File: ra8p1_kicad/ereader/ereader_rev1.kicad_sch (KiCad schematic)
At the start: 0 parts

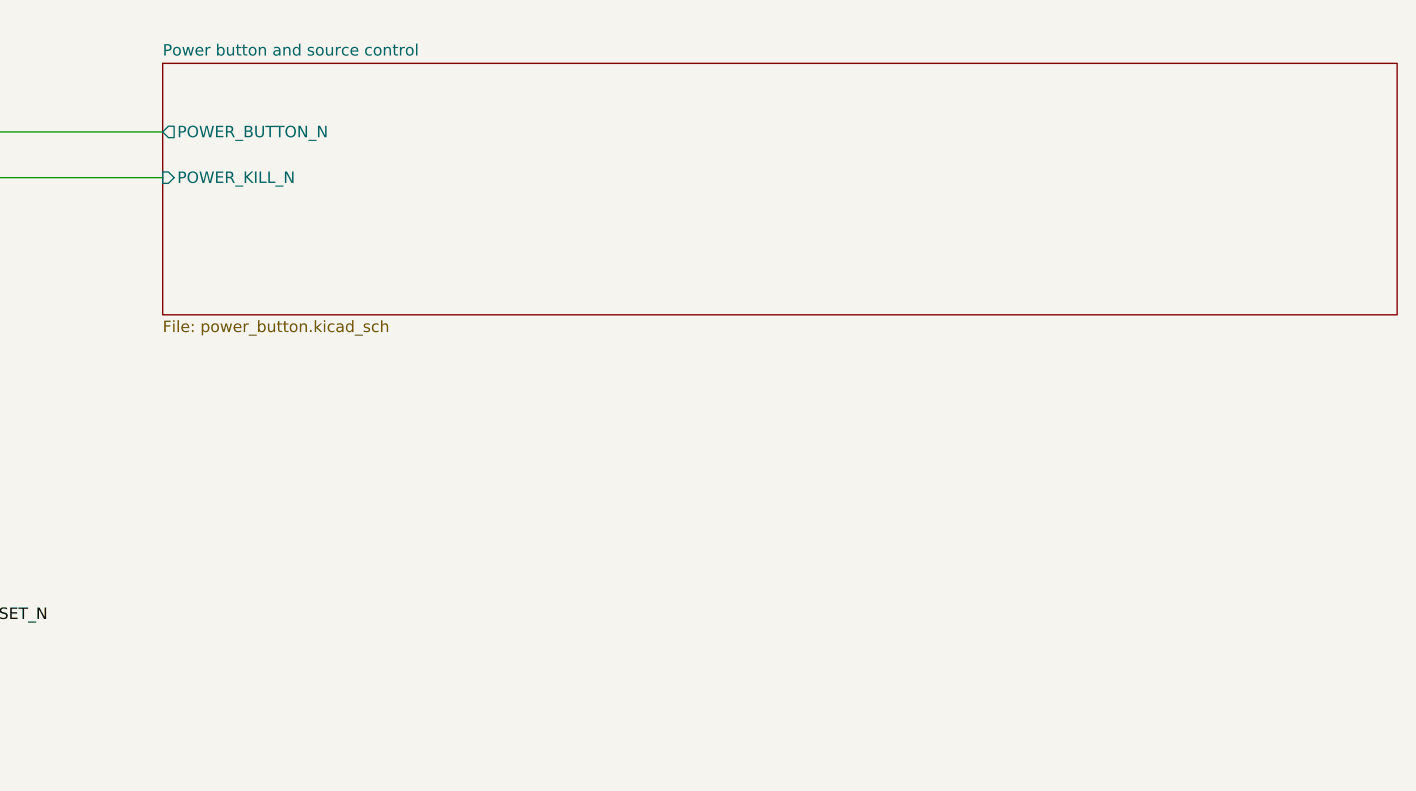
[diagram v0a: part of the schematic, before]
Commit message: Implement main digital supply with linked engineering calculations
Wire the TPS63802 converter and its hierarchical enable, source its exact BOM, and refresh the full nine-page schematic PDF. Preserve the SDRAM pin and timing contract for the memory implementation. Track #825 and #827; system qualification remains open.
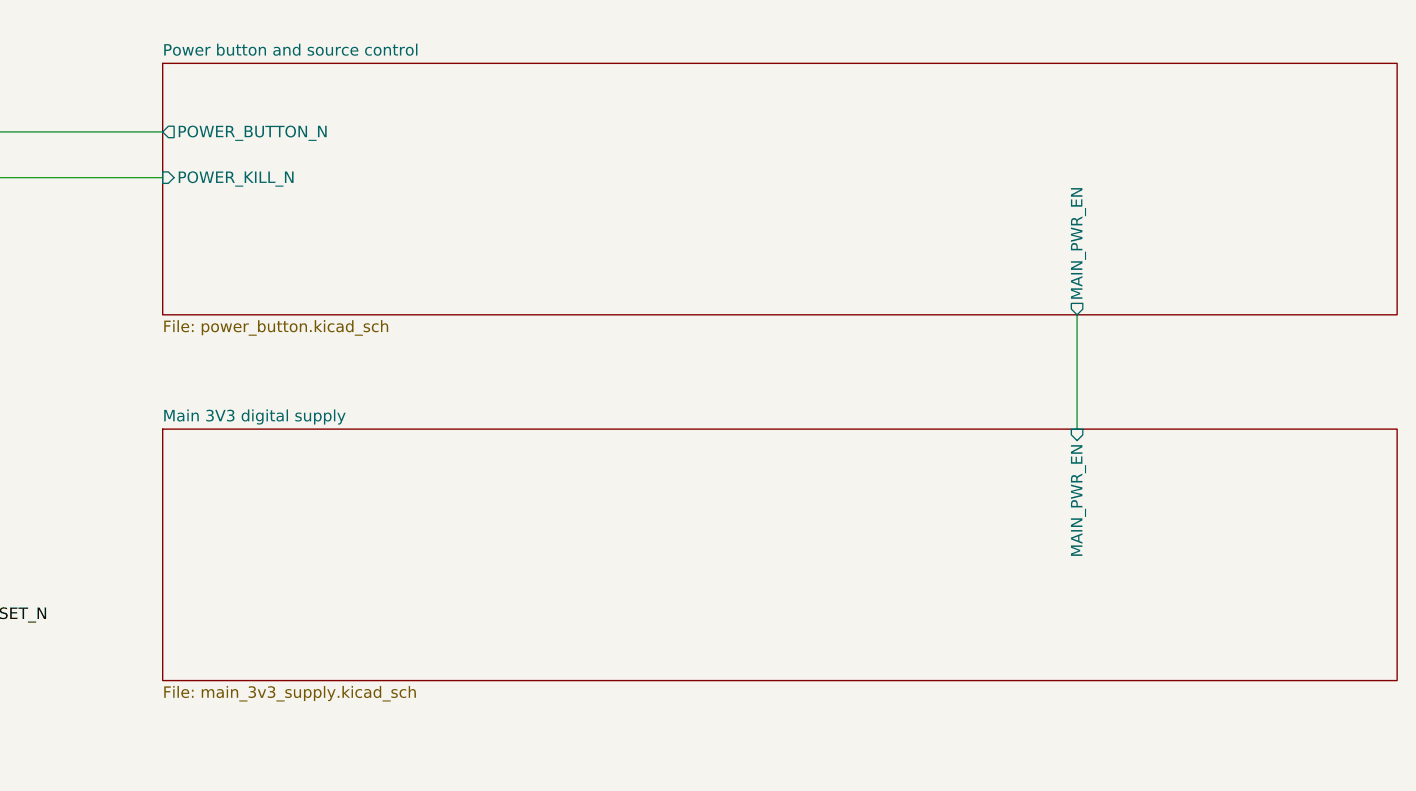
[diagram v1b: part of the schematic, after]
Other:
- added sheet Main 3V3 digital supply (main_3v3_supply.kicad_sch)
- sheet Power button and source control ports: added MAIN_PWR_EN; removed none
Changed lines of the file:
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@@
+	(wire
+		(pts
+			(xy 304.8 205.74) (xy 304.8 218.44)
+		)
+		(stroke
+			(width 0)
+			(type default)
+		)
+	)
 	(wire
 		(pts
@@
 			)
 			(justify right bottom)
+		)
+	)
+	(sheet
+		(at 203.2 218.44)
+		(size 137.16 27.94)
+		(exclude_from_sim no)
+		(in_bom yes)
+		(on_board yes)
+		(dnp no)
+		(fields_autoplaced yes)
+		(stroke
+			(width 0.1524)
+			(type solid)
+		)
+		(fill
+			(color 0 0 0 0)
+		)
+		(property "Sheetname" "Main 3V3 digital supply"
+			(at 203.2 217.7284 0)
+			(show_name no)
+			(do_not_autoplace no)
+			(effects
+				(font
+					(size 1.27 1.27)
+				)
+				(justify left bottom)
+			)
+		)
+		(property "Sheetfile" "main_3v3_supply.kicad_sch"
+			(at 203.2 246.9646 0)
+			(show_name no)
+			(do_not_autoplace no)
+			(effects
+				(font
+					(size 1.27 1.27)
+				)
+				(justify left top)
+			)
+		)
+		(pin "MAIN_PWR_EN" input
+			(at 304.8 218.44 90)
+			(effects
+				(font
+					(size 1.27 1.27)
+				)
+				(justify right)
+			)
+		)
+		(instances
+			(project "ereader_rev1"
+				(path "/0586cc51-9c57-495b-a0c9-c29ba0d48166"
+					(page "9")
+				)
+			)
 		)
 	)
@@
 			(effects
 				(font
+					(size 1.27 1.27)
+				)
+				(justify left)
+			)
+		)
+		(pin "MAIN_PWR_EN" output
+			(at 304.8 205.74 270)
+			(effects
+				(font

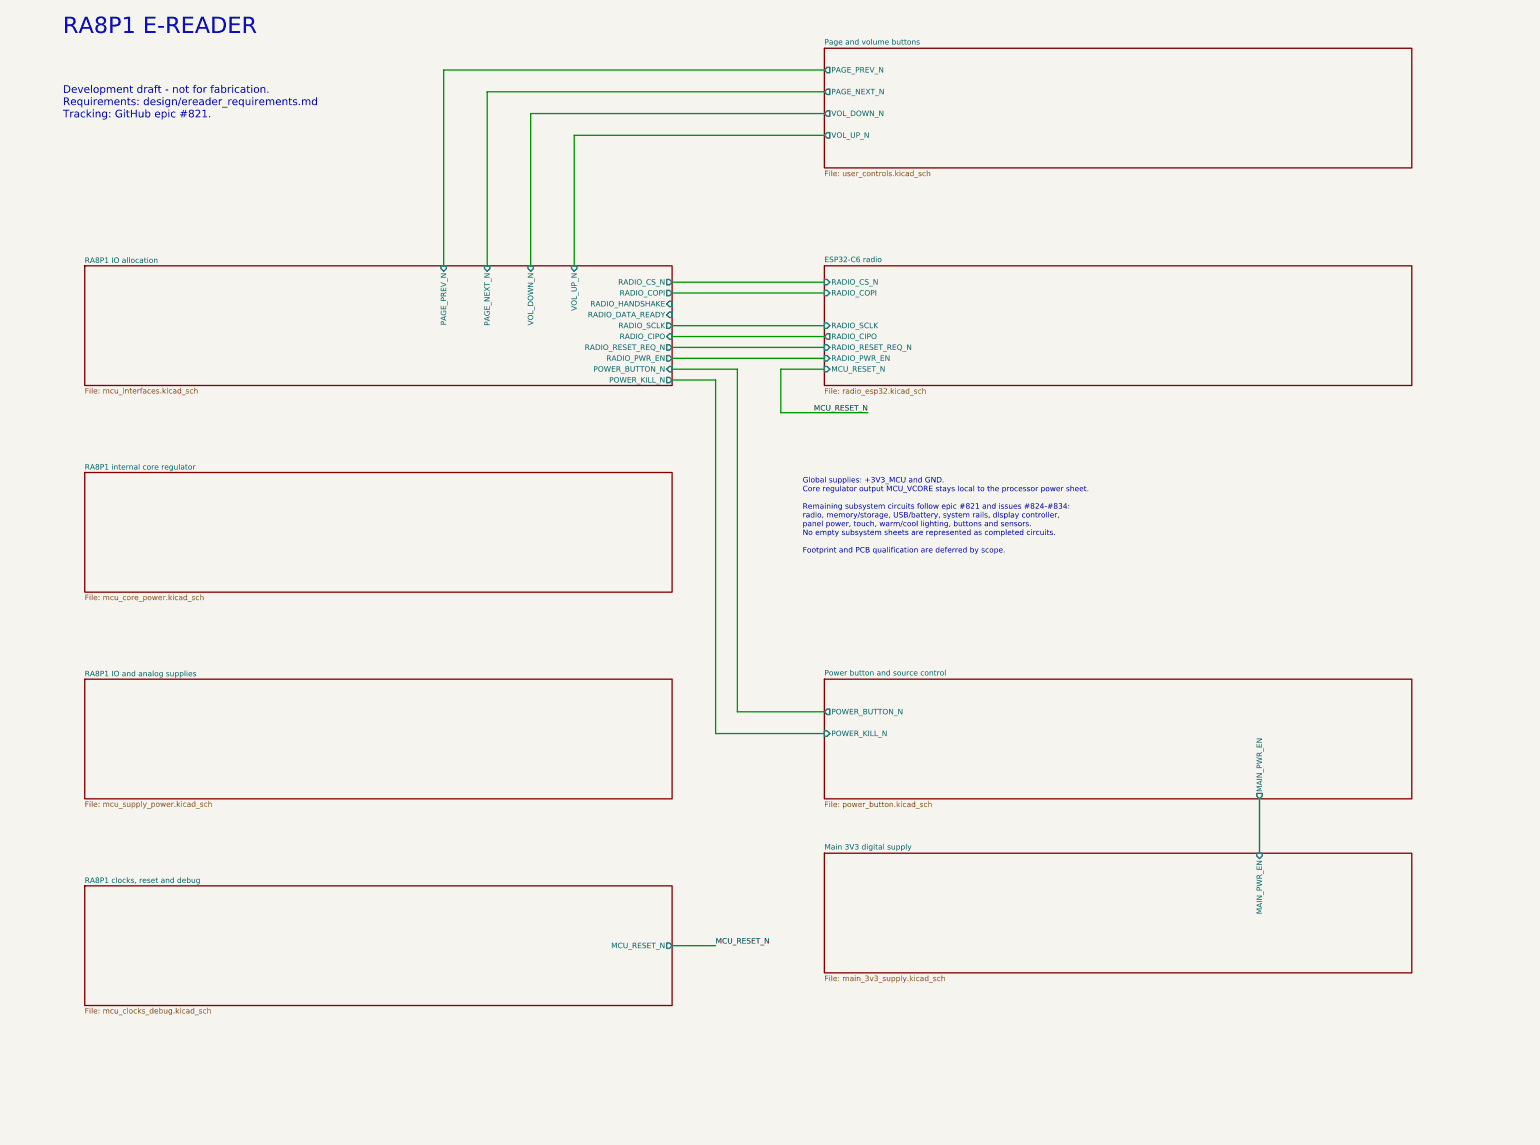
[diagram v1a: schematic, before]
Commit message: Add SDRAM power and bypass schematic phase
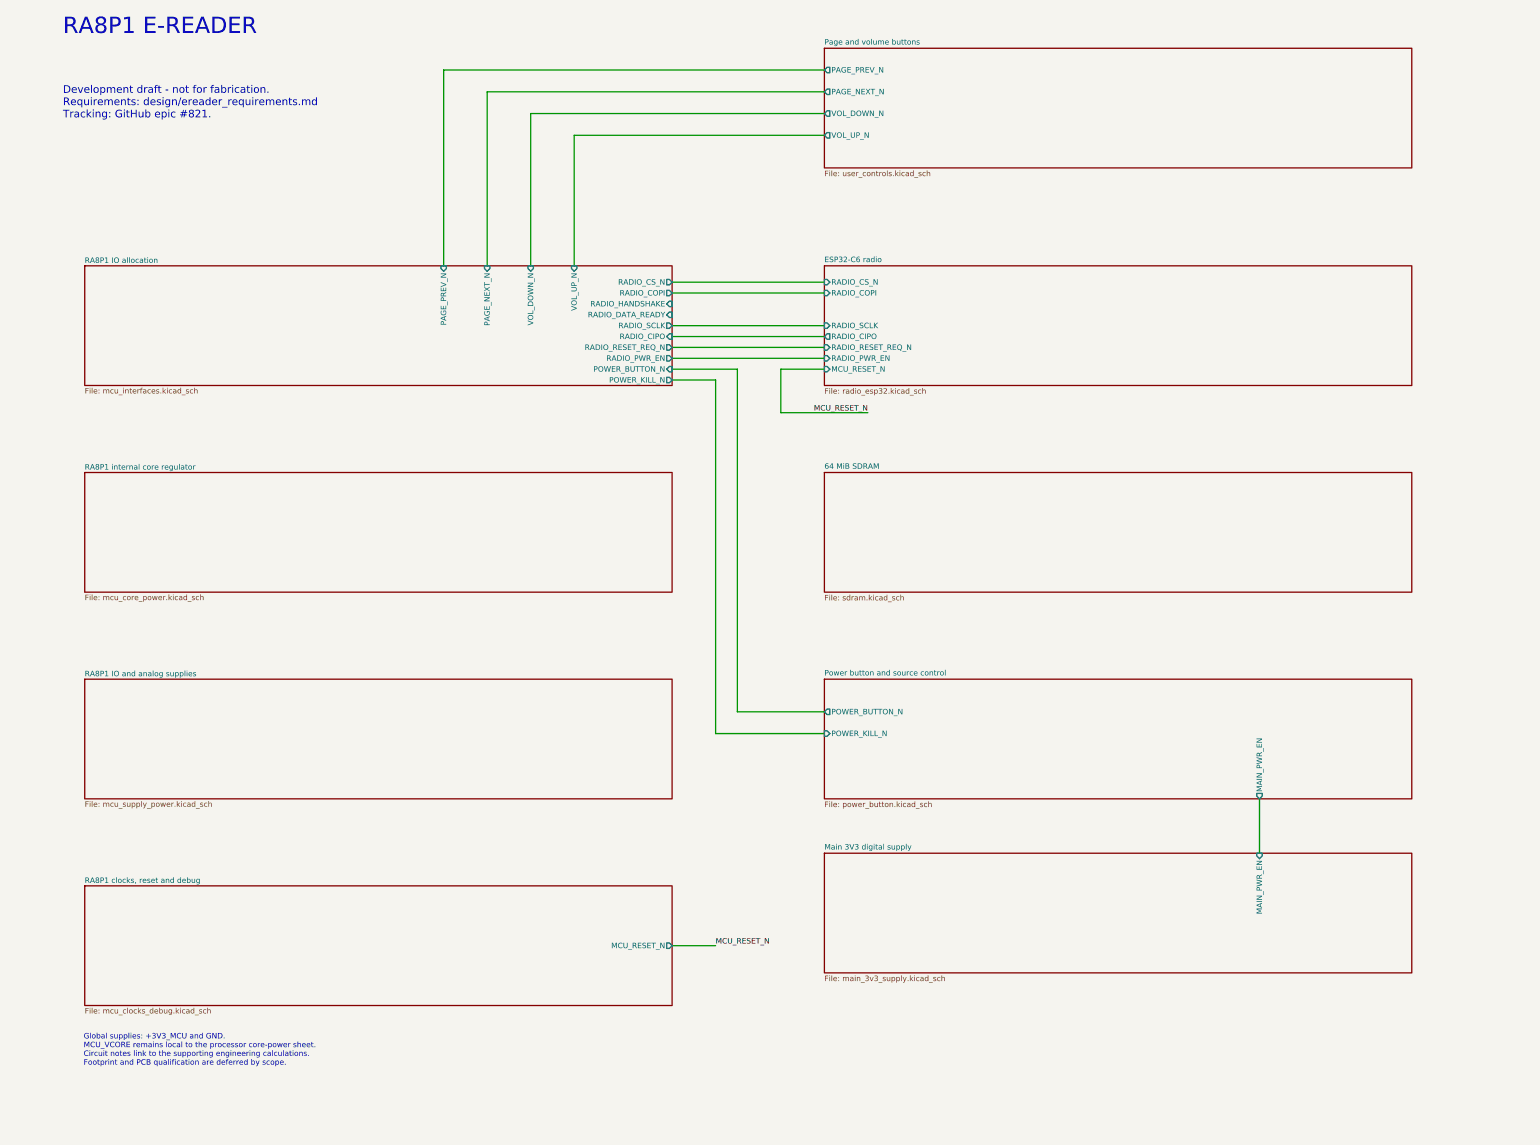
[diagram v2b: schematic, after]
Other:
- added sheet 64 MiB SDRAM (sdram.kicad_sch)
- note added: "Global supplies: +3V3_MCU and GND. MCU_VCORE remains local to the processor core-power sheet. Circuit notes link to the supporting engineering calculations. Footprint and PCB qualification are deferred by scope."
- note removed: "Global supplies: +3V3_MCU and GND. Core regulator output MCU_VCORE stays local to the processor power sheet. Remaining subsystem circuits follow epic #821 and issues #824-#834: radio, memory/storage, USB/battery, system rails, display controller, panel power, touch, warm/cool lighting, buttons and sensors. No empty subsystem sheets are represented as completed circuits. Footprint and PCB qualific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"
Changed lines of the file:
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@@
 		)
 	)
-	(text "Global supplies: +3V3_MCU and GND.\nCore regulator output MCU_VCORE stays local to the processor power sheet.\n\nRemaining subsystem circuits follow epic #821 and issues #824-#834:\nradio, memory/storage, USB/battery, system rails, display controller,\npanel power, touch, warm/cool lighting, buttons and sensors.\nNo empty subsystem sheets are represented as completed circuits.\n\nFootprint and PCB qualification are deferred by scope."
+	(text "Global supplies: +3V3_MCU and GND.\nMCU_VCORE remains local to the processor core-power sheet.\nCircuit notes link to the supporting engineering calculations.\nFootprint and PCB qualification are deferred by scope."
 		(exclude_from_sim no)
-		(at 198.12 139.7 0)
+		(at 30.226 264.414 0)
 		(effects
 			(font
@@
 				)
 			)
+		)
+	)
+	(sheet
+		(at 203.2 129.54)
+		(size 137.16 27.94)
+		(exclude_from_sim no)
+		(in_bom yes)
+		(on_board yes)
+		(dnp no)
+		(fields_autoplaced yes)
+		(stroke
+			(width 0.1524)
+			(type solid)
+		)
+		(fill
+			(color 0 0 0 0)
+		)
+		(property "Sheetname" "64 MiB SDRAM"
+			(at 203.2 128.8284 0)
+			(show_name no)
+			(do_not_autoplace no)
+			(effects
+				(font
+					(size 1.27 1.27)
+				)
+				(justify left bottom)
+			)
+		)
+		(property "Sheetfile" "sdram.kicad_sch"
+			(at 203.2 158.0646 0)
+			(show_name no)
+			(do_not_autoplace no)
+			(effects
+				(font
+					(size 1.27 1.27)
+				)
+				(justify left top)
+			)
+		)
+		(instances
+			(project "ereader_rev1"
+				(path "/0586cc51-9c57-495b-a0c9-c29ba0d48166"
+					(page "10")
+				)
+			)

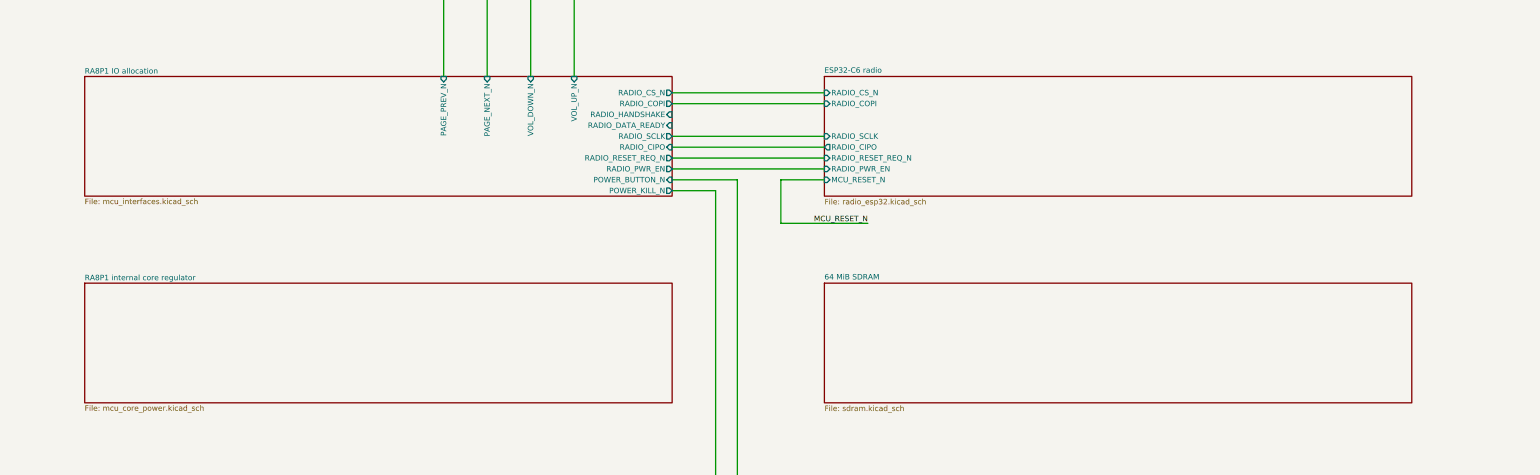
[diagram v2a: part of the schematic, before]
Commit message: Connect SDRAM signals through the schematic hierarchy
Wire the verified 57-signal RA8P1 interface and separate source/load clock nets through R43. Refresh the native BOM, linked CMS-010 contract, and complete ten-page PDF.

ERC: 139 prior findings resolved, zero new identities; 145 errors and two active warnings remain in the unfinished design. MCU pin-role typing, command pullups, and timing qualification remain open under #827.
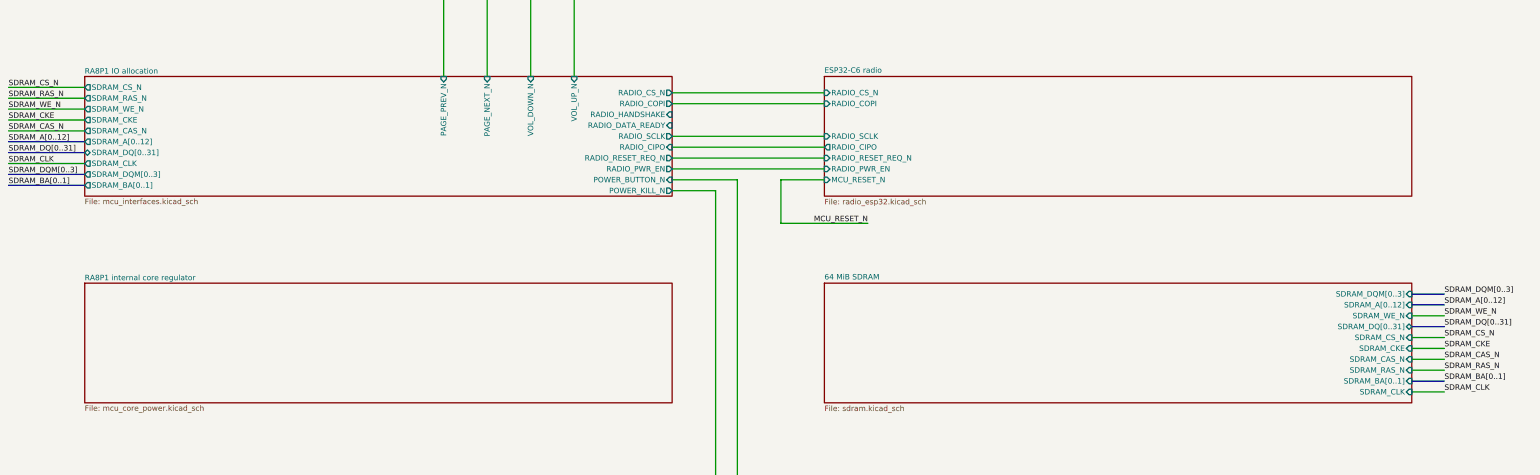
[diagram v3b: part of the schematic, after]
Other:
- sheet 64 MiB SDRAM ports: added SDRAM_A[0..12], SDRAM_BA[0..1], SDRAM_CAS_N, SDRAM_CKE, SDRAM_CLK, SDRAM_CS_N, SDRAM_DQM[0..3], SDRAM_DQ[0..31], SDRAM_RAS_N, SDRAM_WE_N; removed none
- sheet RA8P1 IO allocation ports: added SDRAM_A[0..12], SDRAM_BA[0..1], SDRAM_CAS_N, SDRAM_CKE, SDRAM_CLK, SDRAM_CS_N, SDRAM_DQM[0..3], SDRAM_DQ[0..31], SDRAM_RAS_N, SDRAM_WE_N; removed none

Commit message: Add native Octal NOR supply and bypass checkpoint
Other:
- added sheet 128 MiB Octal NOR (nor_flash.kicad_sch)
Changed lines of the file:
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@@
+	)
+	(sheet
+		(at 30.48 53.34)
+		(size 77.47 20.32)
+		(exclude_from_sim no)
+		(in_bom yes)
+		(on_board yes)
+		(dnp no)
+		(fields_autoplaced yes)
+		(stroke
+			(width 0.1524)
+			(type solid)
+		)
+		(fill
+			(color 0 0 0 0)
+		)
+		(property "Sheetname" "128 MiB Octal NOR"
+			(at 30.48 52.6284 0)
+			(show_name no)
+			(do_not_autoplace no)
+			(effects
+				(font
+					(size 1.27 1.27)
+				)
+				(justify left bottom)
+			)
+		)
+		(property "Sheetfile" "nor_flash.kicad_sch"
+			(at 30.48 74.2446 0)
+			(show_name no)
+			(do_not_autoplace no)
+			(effects
+				(font
+					(size 1.27 1.27)
+				)
+				(justify left top)
+			)
+		)
+		(instances
+			(project "ereader_rev1"
+				(path "/0586cc51-9c57-495b-a0c9-c29ba0d48166"
+					(page "11")
+				)
+			)
+		)
 	)
 	(sheet
